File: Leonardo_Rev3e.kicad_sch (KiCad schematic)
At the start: 56 parts, among them IC1 REG1117-5, IC2 LMV358IDGKR, J1 USBMICRO, J2 8x1F-H8.5, J3 8x1F-H8.5, J4 6x1F-H8.5, T1 FDN340P, U1 ATMEGA32U4-XUMU, U2 ATMEGA32U4-XUAU, U3 LP2985-33DBVR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

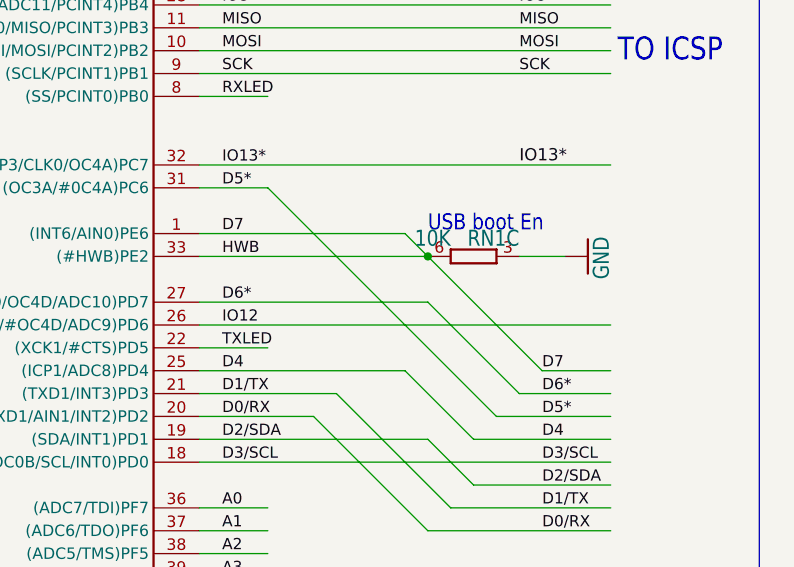
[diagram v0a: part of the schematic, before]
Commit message: BUG: Correct D7/HWB error and upgrade to Kicad 7
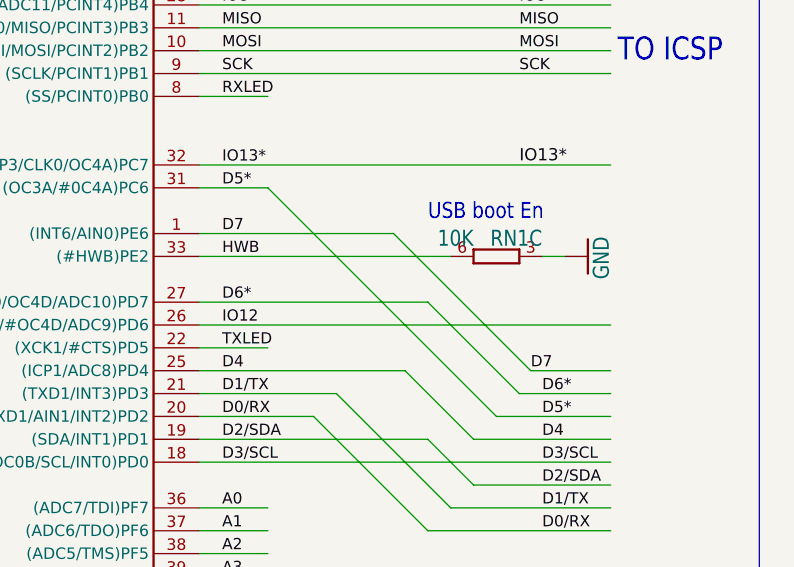
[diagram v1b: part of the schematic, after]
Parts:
- C1, C11, C13, C14, C2, C22, C3, C4, C5, C6, C7, C9: footprint Leonardo_Rev3d:C0603-ROUND -> Leonardo_Rev3e:C0603-ROUND; symbol Leonardo_Rev3d:C-EUC0603 -> Leonardo_Rev3e:C-EUC0603
- C10, C12, C8: footprint Leonardo_Rev3d:SMC_B -> Leonardo_Rev3e:SMC_B; symbol Leonardo_Rev3d:CPOL-EUSMCB -> Leonardo_Rev3e:CPOL-EUSMCB
- D+0, D-0, GND0, VUSB0: footprint Leonardo_Rev3d:TP-1.00MM -> Leonardo_Rev3e:TP-1.00MM; symbol Leonardo_Rev3d:TPTP-1.00MM -> Leonardo_Rev3e:TPTP-1.00MM
- D1: footprint Leonardo_Rev3d:SMB -> Leonardo_Rev3e:SMB; symbol Leonardo_Rev3d:DIODE-SMB -> Leonardo_Rev3e:DIODE-SMB
- D2: footprint Leonardo_Rev3d:MINIMELF -> Leonardo_Rev3e:MINIMELF; symbol Leonardo_Rev3d:DIODE-MINIMELF -> Leonardo_Rev3e:DIODE-MINIMELF
- EXTPOWER0: footprint Leonardo_Rev3d:POWERSUPPLY_DC-21MM -> Leonardo_Rev3e:POWERSUPPLY_DC-21MM; symbol Leonardo_Rev3d:POWERSUPPLY_DC21MMX -> Leonardo_Rev3e:POWERSUPPLY_DC21MMX
- F1: footprint Leonardo_Rev3d:L1812 -> Leonardo_Rev3e:L1812; symbol Leonardo_Rev3d:L-EUL1812 -> Leonardo_Rev3e:L-EUL1812
- FID1, FID2, FID3: footprint Leonardo_Rev3d:FD-1-1.5 -> Leonardo_Rev3e:FD-1-1.5; symbol Leonardo_Rev3d:FIDUCIAL-1.5MM -> Leonardo_Rev3e:FIDUCIAL-1.5MM
- IC1: footprint Leonardo_Rev3d:SOT223 -> Leonardo_Rev3e:SOT223; symbol Leonardo_Rev3d:MC33269ST -> Leonardo_Rev3e:MC33269ST
- IC2: footprint Leonardo_Rev3d:MSOP08 -> Leonardo_Rev3e:MSOP08; symbol Leonardo_Rev3d:LMV358?MM -> Leonardo_Rev3e:LMV358?MM
- ICSP0: footprint Leonardo_Rev3d:2X03 -> Leonardo_Rev3e:2X03; symbol Leonardo_Rev3d:PINHD-2X3 -> Leonardo_Rev3e:PINHD-2X3
- J1: footprint Leonardo_Rev3d:10118194-0001LF -> Leonardo_Rev3e:10118194-0001LF; symbol Leonardo_Rev3d:USBMICRO -> Leonardo_Rev3e:USBMICRO
- J2, J3: footprint Leonardo_Rev3d:1X08 -> Leonardo_Rev3e:1X08; symbol Leonardo_Rev3d:PINHD-1X8 -> Leonardo_Rev3e:PINHD-1X8
- J4: footprint Leonardo_Rev3d:1X06 -> Leonardo_Rev3e:1X06; symbol Leonardo_Rev3d:PINHD-1X6 -> Leonardo_Rev3e:PINHD-1X6
- JP1: footprint Leonardo_Rev3d:1X10 -> Leonardo_Rev3e:1X10; symbol Leonardo_Rev3d:PINHD-1X10 -> Leonardo_Rev3e:PINHD-1X10
- JP2: footprint Leonardo_Rev3d:HEADER_2_2.54 -> Leonardo_Rev3e:HEADER_2_2.54; symbol Leonardo_Rev3d:Jumper_2_Open -> Leonardo_Rev3e:Jumper_2_Open
- L0, ON0, RX0, TX0: footprint Leonardo_Rev3d:CHIPLED_0805 -> Leonardo_Rev3e:CHIPLED_0805; symbol Leonardo_Rev3d:LEDCHIPLED_0805 -> Leonardo_Rev3e:LEDCHIPLED_0805
- L1, L2: footprint Leonardo_Rev3d:0805 -> Leonardo_Rev3e:0805; symbol Leonardo_Rev3d:WE-CBF_0805 -> Leonardo_Rev3e:WE-CBF_0805
- R1, R4: footprint Leonardo_Rev3d:R0603-ROUND -> Leonardo_Rev3e:R0603-ROUND; symbol Leonardo_Rev3d:R-EU_R0603 -> Leonardo_Rev3e:R-EU_R0603
- R2, R3: footprint Leonardo_Rev3d:R0402 -> Leonardo_Rev3e:R0402; symbol Leonardo_Rev3d:R-EU_R0402 -> Leonardo_Rev3e:R-EU_R0402
- RESET0: footprint Leonardo_Rev3d:TS07 -> Leonardo_Rev3e:TS07; symbol Leonardo_Rev3d:TS07 -> Leonardo_Rev3e:TS07
- RN1, RN2, RN3: footprint Leonardo_Rev3d:CAY16 -> Leonardo_Rev3e:CAY16; symbol Leonardo_Rev3d:4R-NCAY16 -> Leonardo_Rev3e:4R-NCAY16
- T1: footprint Leonardo_Rev3d:SOT-23 -> Leonardo_Rev3e:SOT-23; symbol Leonardo_Rev3d:PMOSSOT23 -> Leonardo_Rev3e:PMOSSOT23
- U1: footprint Leonardo_Rev3d:QFN44ML7X7 -> Leonardo_Rev3e:QFN44ML7X7; symbol Leonardo_Rev3d:ATMEGA32U4-XUMU -> Leonardo_Rev3e:ATMEGA32U4-XUMU
- U2: footprint Leonardo_Rev3d:TQFP44-PAD -> Leonardo_Rev3e:TQFP44-PAD; symbol Leonardo_Rev3d:ATMEGA32U4-XUAU -> Leonardo_Rev3e:ATMEGA32U4-XUAU
- U3: footprint Leonardo_Rev3d:SOT23-DBV -> Leonardo_Rev3e:SOT23-DBV; symbol Leonardo_Rev3d:LP2985-XXDBVR -> Leonardo_Rev3e:LP2985-XXDBVR
- Y1: footprint Leonardo_Rev3d:CRYSTAL-3.2-2.5 -> Leonardo_Rev3e:CRYSTAL-3.2-2.5; symbol Leonardo_Rev3d:CRYSTAL-3.2-2.5 -> Leonardo_Rev3e:CRYSTAL-3.2-2.5
- Z1, Z2: footprint Leonardo_Rev3d:CT_CN0603 -> Leonardo_Rev3e:CT_CN0603; symbol Leonardo_Rev3d:VARISTORCN0603 -> Leonardo_Rev3e:VARISTORCN0603
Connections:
- net D7: no longer RN1.6 (2), U1.33 ((#HWB)PE2), U2.33 ((#HWB)PE2)
- new net HWB: RN1.6 (2), U1.33 ((#HWB)PE2), U2.33 ((#HWB)PE2)
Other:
- moved on the sheet: RN1C
